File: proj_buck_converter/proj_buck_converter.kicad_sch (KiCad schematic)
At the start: 1 part

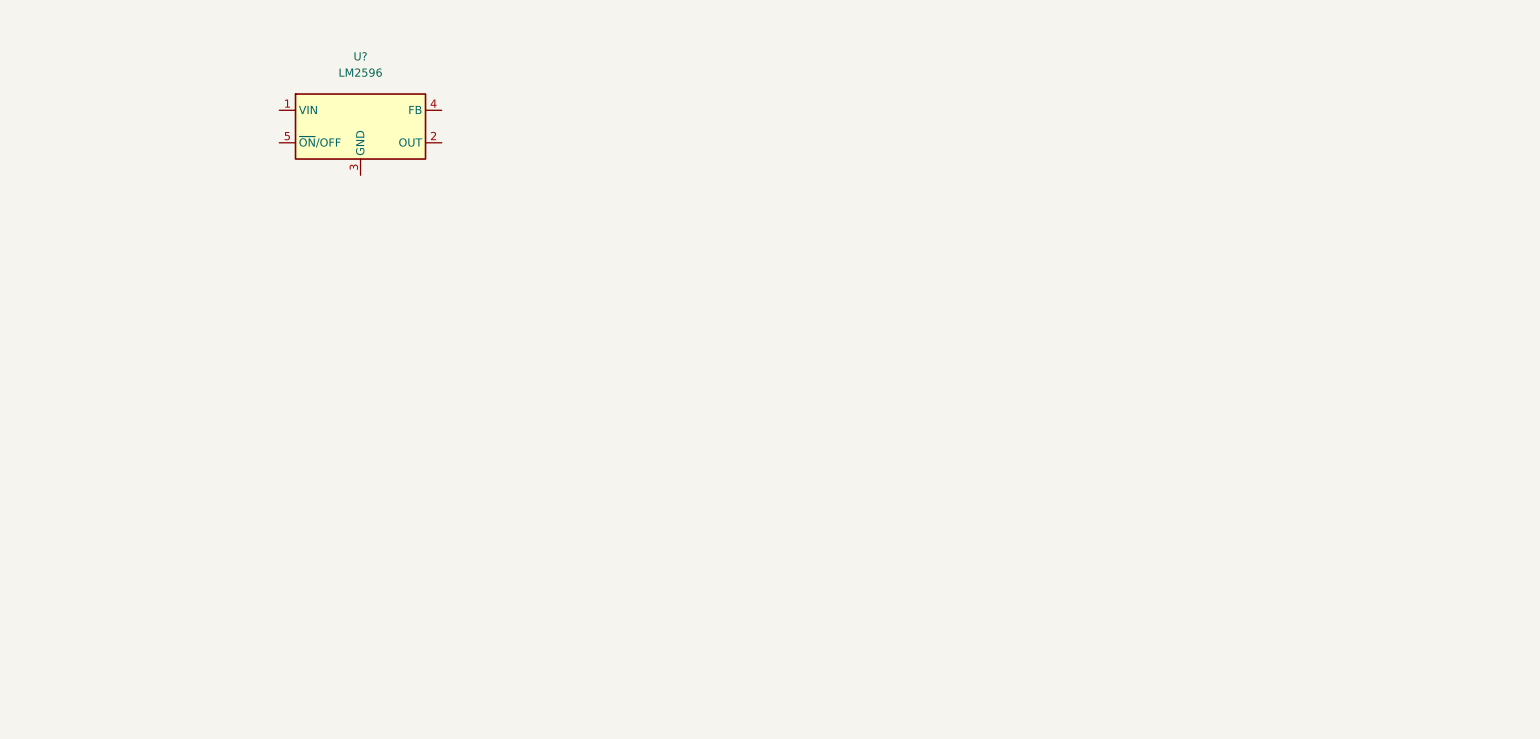
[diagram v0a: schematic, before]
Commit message: added library parts and sub sheet
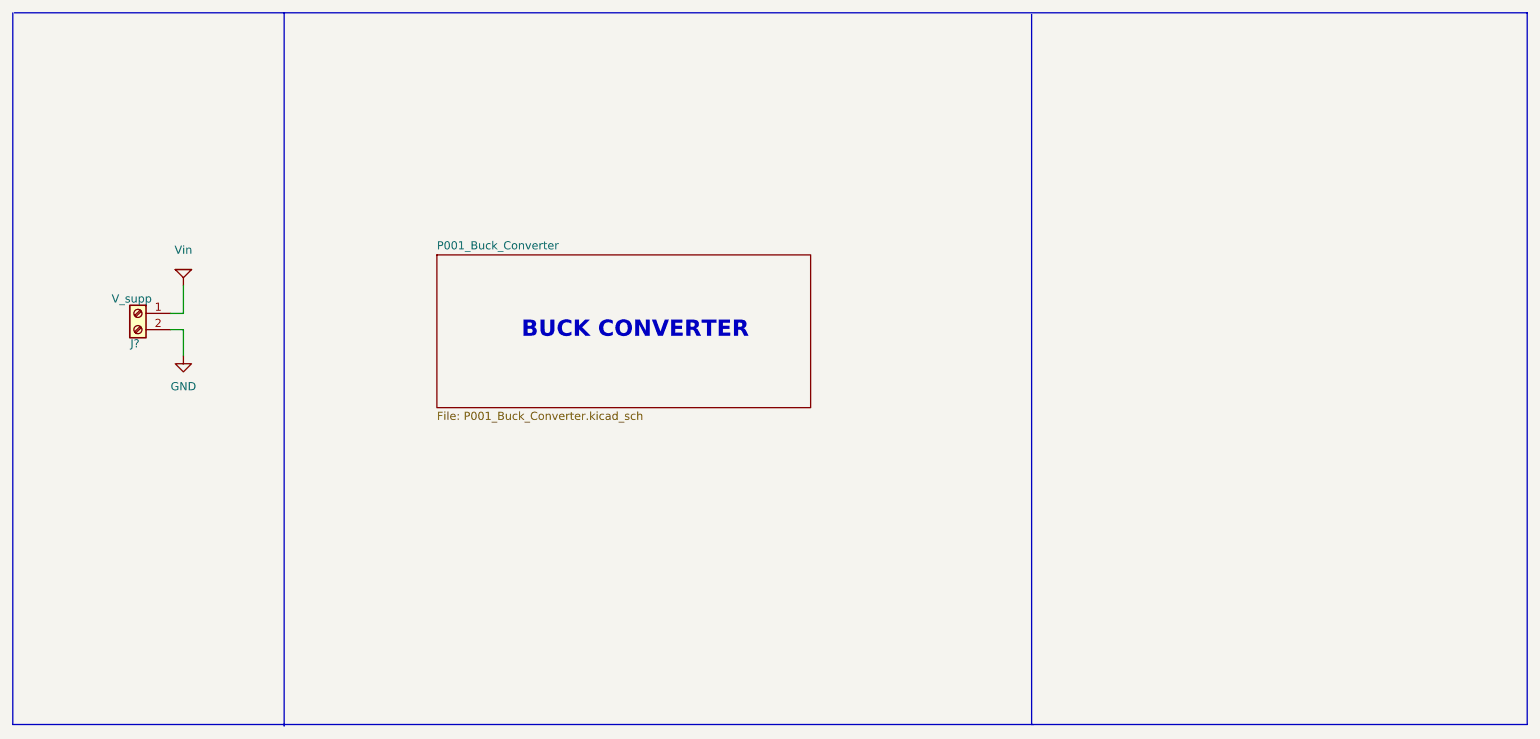
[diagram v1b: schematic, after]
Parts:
- removed U?: LM2596, symbol buck_converter_lib:LM2596
- added J?: V_supp, symbol Connector:Screw_Terminal_01x02
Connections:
- new net GND: J?.2 (Pin_2)
- new net Vin: J?.1 (Pin_1)
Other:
- added sheet P001_Buck_Converter (P001_Buck_Converter.kicad_sch)
- note added: "BUCK CONVERTER"
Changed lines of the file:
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@@
 (kicad_sch (version 20211123) (generator eeschema)
   (paper "A4")
-  (symbol (lib_id "buck_converter_lib:LM2596") (at 86.36 56.642 0) (unit 1)
+  (polyline (pts (xy 268.732 150.114) (xy 32.004 150.114))
+    (stroke (width 0) (type default) (color 0 0 0 0))
+  )
+  (wire (pts (xy 58.674 85.852) (xy 56.642 85.852))
+    (stroke (width 0) (type default) (color 0 0 0 0))
+  )
+  (wire (pts (xy 56.642 88.392) (xy 58.674 88.392))
+    (stroke (width 0) (type default) (color 0 0 0 0))
+  )
+  (polyline (pts (xy 32.004 38.862) (xy 32.004 150.114))
+    (stroke (width 0) (type default) (color 0 0 0 0))
+  )
+  (polyline (pts (xy 32.258 38.862) (xy 268.732 38.862))
+    (stroke (width 0) (type default) (color 0 0 0 0))
+  )
+  (polyline (pts (xy 74.422 38.862) (xy 74.422 150.368))
+    (stroke (width 0) (type default) (color 0 0 0 0))
+  )
+  (wire (pts (xy 58.674 88.392) (xy 58.674 92.456))
+    (stroke (width 0) (type default) (color 0 0 0 0))
+  )
+  (polyline (pts (xy 268.732 38.862) (xy 268.732 150.114))
+    (stroke (width 0) (type default) (color 0 0 0 0))
+  )
+  (wire (pts (xy 58.674 81.534) (xy 58.674 85.852))
+    (stroke (width 0) (type default) (color 0 0 0 0))
+  )
+  (polyline (pts (xy 191.262 150.114) (xy 191.516 150.114))
+    (stroke (width 0) (type default) (color 0 0 0 0))
+  )
+  (polyline (pts (xy 191.262 39.116) (xy 191.262 150.114))
+    (stroke (width 0) (type default) (color 0 0 0 0))
+  )
+  (text "BUCK CONVERTER" (at 111.506 89.916 0)
+    (effects (font (size 2.54 2.54) (thickness 0.254) bold) (justify left bottom))
+  )
+  (symbol (lib_id "power:GND") (at 58.674 92.456 0) (unit 1)
     (in_bom yes) (on_board yes) (fields_autoplaced)
-    (property "Reference" "U?" (id 0) (at 86.36 45.72 0))
-    (property "Value" "LM2596" (id 1) (at 86.36 48.26 0))
-    (property "Footprint" "" (id 2) (at 86.36 56.642 0)
+    (property "Reference" "#PWR?" (id 0) (at 58.674 98.806 0)
       (effects (font (size 1.27 1.27)) hide)
     )
-    (property "Datasheet" "" (id 3) (at 86.36 56.642 0)
+    (property "Value" "GND" (id 1) (at 58.674 97.282 0))
+    (property "Footprint" "" (id 2) (at 58.674 92.456 0)
+      (effects (font (size 1.27 1.27)) hide)
+    )
+    (property "Datasheet" "" (id 3) (at 58.674 92.456 0)
+      (effects (font (size 1.27 1.27)) hide)
+    )
+    (pin "1")
+  )
+  (symbol (lib_id "Supply:Vin") (at 58.674 81.534 0) (unit 1)
+    (in_bom yes) (on_board yes) (fields_autoplaced)
+    (property "Reference" "#PWR?" (id 0) (at 58.674 84.074 0)
+      (effects (font (size 1.27 1.27)) hide)
+    )
+    (property "Value" "Vin" (id 1) (at 58.674 75.946 0))
+    (property "Footprint" "" (id 2) (at 56.134 82.804 0)
+      (effects (font (size 1.27 1.27)) hide)
+    )
+    (property "Datasheet" "" (id 3) (at 58.674 81.534 0)
+      (effects (font (size 1.27 1.27)) hide)
+    )
+    (pin "1")
+  )
+  (symbol (lib_id "Connector:Screw_Terminal_01x02") (at 51.562 85.852 0) (mirror y) (unit 1)
+    (in_bom yes) (on_board yes)
+    (property "Reference" "J?" (id 0) (at 51.1048 90.5764 0))
+    (property "Value" "V_supp" (id 1) (at 50.5968 83.566 0))
+    (property "Footprint" "" (id 2) (at 51.562 85.852 0)
+      (effects (font (size 1.27 1.27)) hide)
+    )
+    (property "Datasheet" "~" (id 3) (at 51.562 85.852 0)
       (effects (font (size 1.27 1.27)) hide)
     )
     (pin "1")
     (pin "2")
-    (pin "3")
-    (pin "4")
-    (pin "5")
+  )
+  (sheet (at 98.298 76.708) (size 58.42 23.876) (fields_autoplaced)
+    (stroke (width 0.1524) (type solid) (color 0 0 0 0))
+    (fill (color 255 249 173 1.0000))
+    (property "Sheet name" "P001_Buck_Converter" (id 0) (at 98.298 75.9964 0)
+      (effects (font (size 1.27 1.27)) (justify left bottom))
+    )
+    (property "Sheet file" "P001_Buck_Converter.kicad_sch" (id 1) (at 98.298 101.1686 0)
+      (effects (font (size 1.27 1.27)) (justify left top))
+    )
   )
   (sheet_instances
     (path "/" (page "1"))
+    (path "/c4bd05a8-c41c-455b-9aba-6f4047b7569b" (page "2"))
   )
   (symbol_instances
-    (path "/875187fa-6b66-4b37-a9ff-34492e116e33"
-      (reference "U?") (unit 1) (value "LM2596") (footprint "")
+    (path "/3ac6404c-b5e8-487a-a9af-11f395f4cf2e"
+      (reference "#PWR?") (unit 1) (value "GND") (footprint "")
+    )
+    (path "/5c4d61e2-929b-41f5-8c05-c6fb8daf3423"
+      (reference "#PWR?") (unit 1) (value "Vin") (footprint "")
+    )
+    (path "/73fe496d-284a-468e-8764-7b37123038ca"
+      (reference "J?") (unit 1) (value "V_supp") (footprint "")
+    )
+    (path "/c4bd05a8-c41c-455b-9aba-6f4047b7569b/6a77bbf3-291c-404f-96b7-d869320cc7e0"
+      (reference "U?") (unit 1) (value "LM2596") (footprint "Package_TO_SOT_SMD:TO-263-5_TabPin6")
     )
   )
